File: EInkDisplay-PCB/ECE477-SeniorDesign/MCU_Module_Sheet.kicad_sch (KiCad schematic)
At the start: 25 parts, among them SW1 SW_Push_Dual_x2, U3 STM32L496ZGTxP, Y1 32.768kHz

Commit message: 0805
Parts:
- C19: footprint (none) -> Capacitor_SMD:C_0805_2012Metric_Pad1.18x1.45mm_HandSolder
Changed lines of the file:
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@@
 			)
 		)
-		(property "Footprint" ""
+		(property "Footprint" "Capacitor_SMD:C_0805_2012Metric_Pad1.18x1.45mm_HandSolder"
 			(at 179.07 34.29 0)
 			(effects

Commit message: change
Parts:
- added J7: Conn_01x05, symbol Connector_Generic:Conn_01x05
- ABS04W-32.768KHZ-4-D2-T5: renamed from Y1; footprint (none) -> PCB_Lib:XTAL_ABS04W-32.768KHZ-4-D2-T5
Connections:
- net NRST: now also J7.3 (Pin_3)
- net SWDIO: now reaches U3.105 (PA13)
- net SWDIO: now also J7.4 (Pin_4)
- net SWCLK: now reaches U3.109 (PA14)
- net SWCLK: now also J7.5 (Pin_5)

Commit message: push
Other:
- note added: "consider pull up"
- note removed: "force reset"
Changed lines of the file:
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@@
 		)
 	)
-	(text "force reset\n"
+	(text "consider pull up"
 		(exclude_from_sim no)
 		(at 143.764 44.958 0)

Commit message: Lotta changes
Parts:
- removed SW1: SW_Push_Dual_x2, symbol Switch:SW_Push_Dual_x2
- added J8: Conn_01x05, symbol Connector_Generic:Conn_01x05
- added TP17, TP18, TP19, TP20, TP21, TP22, TP23, TP24, TP25, TP26, TP27, TP28, TP29, TP30, TP31, TP32: ~, symbol Connector:TestPoint
- added U7: PTS526 SK15 SMTR2 LFS, PCB_Lib:PTS256, symbol EinkComponentLibrary:PTS526_SK15_SMTR2_LFS
- C1, C10, C11, C12, C13, C14, C15, C16, C17, C18, C2, C20, C3, C4, C9: footprint (none) -> Capacitor_SMD:C_0805_2012Metric_Pad1.18x1.45mm_HandSolder
- C28, C29: value 20pF -> 4pF; footprint (none) -> Capacitor_SMD:C_0805_2012Metric_Pad1.18x1.45mm_HandSolder
- SWBOOT0: value SW_SPDT -> PCM12SMTR; footprint (none) -> PCB_Lib:PCM12SMTR_CNK
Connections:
- net GND: now also U7.2
- net NRST: now also U7.1
- net button1: now also TP30.1
- net button2: now also TP31.1
- net button3: now also TP32.1
- net Extra_3: now reaches U3.1 (PE2)
- net Extra_3: now also J8.3 (Pin_3), TP27.1
- net USART2_TX: now reaches U3.119 (PD5)
- net USART2_TX: now also TP21.1
- net USART2_RX: now reaches U3.122 (PD6)
- net USART2_RX: now also TP22.1
- net SPI3_SCK: now reaches U3.124 (PG9)
- net SPI3_SCK: now also TP17.1
- net SPI3_MISO: now reaches U3.125 (PG10)
- net SPI3_MISO: now also TP18.1
- net SPI3_MOSI: now reaches U3.126 (PG11)
- net SPI3_MOSI: now also TP19.1
- net SPI3_NSS: now reaches U3.127 (PG12)
- net SPI3_NSS: now also TP20.1
- net Extra_1: now reaches U3.140 (PE0)
- net Extra_1: now also J8.1 (Pin_1), TP25.1
- net Extra_2: now reaches U3.141 (PE1)
- net Extra_2: now also J8.2 (Pin_2), TP26.1
- net Extra_4: now reaches U3.2 (PE3)
- net Extra_4: now also J8.4 (Pin_4), TP28.1
- net Extra_5: now reaches U3.3 (PE4)
- net Extra_5: now also J8.5 (Pin_5), TP29.1
- net I2C4_SCL: now reaches U3.81 (PD12)
- net I2C4_SCL: now also TP23.1
- net I2C4_SDA: now reaches U3.82 (PD13)
- net GPIO_1 renamed I2C2_SDA
- net GPIO_2 renamed I2C2_SCL
- no-connect marks 90 -> 79
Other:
- note added: "Extra Comms"
- note added: "Extra GPIOs"
- note added: "Extra SPI"
- note added: "Programming Header"
- moved on the sheet: J7

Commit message: onto PCB
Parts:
- removed ABS04W-32.768KHZ-4-D2-T5: 32.768kHz, PCB_Lib:XTAL_ABS04W-32.768KHZ-4-D2-T5, symbol Device:Crystal
- removed TP24: ~, symbol Connector:TestPoint
- added Y1: Y1, PCB_Lib:XTAL_ABS04W-32.768KHZ-4-D2-T5, symbol Device:Crystal_GND24_Small
- C1, C10, C11, C12, C13, C14, C15, C17, C18, C19, C2, C3, C4, C9: footprint Capacitor_SMD:C_0805_2012Metric_Pad1.18x1.45mm_HandSolder -> Capacitor_SMD:C_0603_1608Metric_Pad1.08x0.95mm_HandSolder
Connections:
- net GND: now also Y1.2
- net GPIO_3: now also U3.80 (PD11); no longer U3.12 (PF2)
- net GPIO_4: now also U3.79 (PD10); no longer U3.13 (PF3)
- net GPIO_5: now also U3.78 (PD9); no longer U3.14 (PF4)
- net GPIO_6: now also U3.77 (PD8); no longer U3.15 (PF5)
- net I2C2_SCL: now also TP23.1, U3.81 (PD12); no longer U3.11 (PF1)
- net I2C2_SDA: now also U3.82 (PD13); no longer U3.10 (PF0)
- net I2C4_SCL: now also U3.11 (PF1); no longer TP23.1, U3.81 (PD12)
- net I2C4_SDA: now also U3.10 (PF0); no longer U3.82 (PD13)
- net at C28.2, U3.23 (PH0): now also Y1.1
- net at C29.2, U3.24 (PH1): now also Y1.3
- no-connect marks 79 -> 80
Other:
- note removed: "Extra Comms"
- moved on the sheet: C28, C29, U7

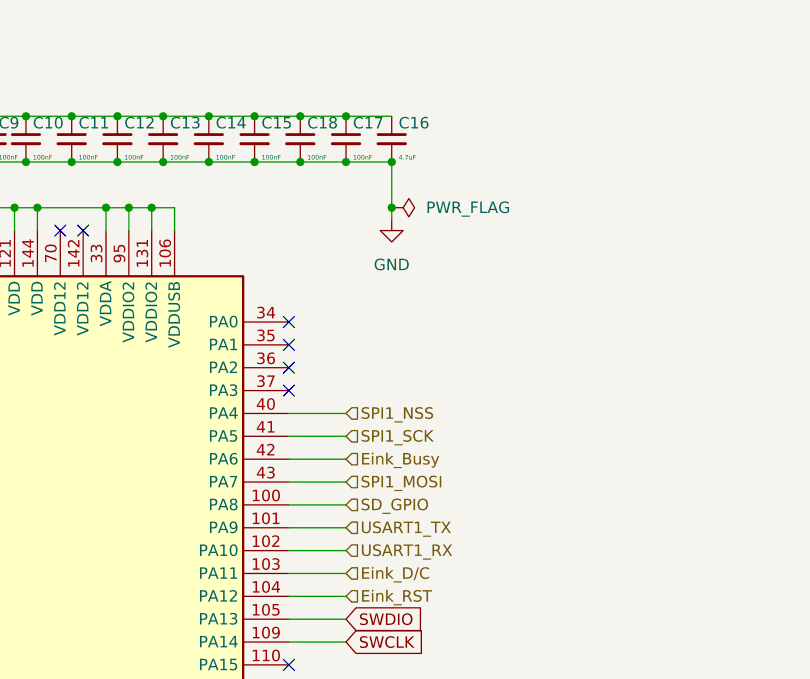
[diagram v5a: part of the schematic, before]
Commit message: SD card updates
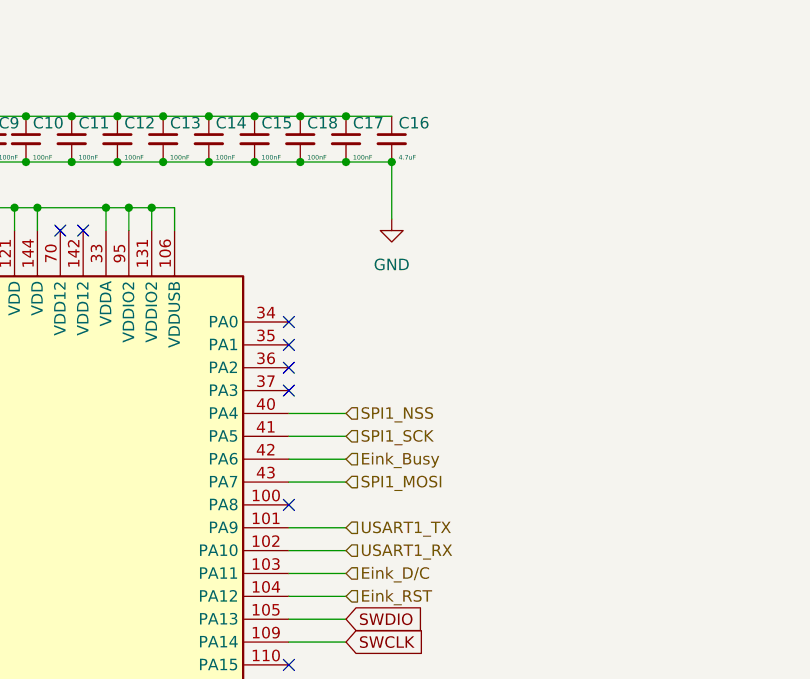
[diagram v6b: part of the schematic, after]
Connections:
- net SD_GPIO: no longer names the net of U3.100 (PA8)
- no-connect marks 80 -> 81
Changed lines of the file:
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@@
 	)
 	(junction
-		(at 243.84 41.91)
-		(diameter 0)
-		(color 0 0 0 0)
-	)
-	(junction
 		(at 121.92 111.76)
 		(diameter 0)
@@
 	)
 	(no_connect
+		(at 232.41 74.93)
+	)
+	(no_connect
 		(at 166.37 135.89)
 	)
@@
 	(wire
 		(pts
-			(xy 243.84 36.83) (xy 243.84 41.91)
+			(xy 243.84 36.83) (xy 243.84 43.18)
 		)
 		(stroke
@@
 	(wire
 		(pts
-			(xy 232.41 74.93) (xy 238.76 74.93)
-		)
-		(stroke
-			(width 0)
-			(type default)
-		)
-	)
-	(wire
-		(pts
 			(xy 232.41 130.81) (xy 241.3 130.81)
 		)
@@
 	(wire
 		(pts
-			(xy 243.84 41.91) (xy 243.84 43.18)
-		)
-		(stroke
-			(width 0)
-			(type default)
-		)
-	)
-	(wire
-		(pts
 			(xy 146.05 64.77) (xy 146.05 67.31)
 		)
@@
 		)
 	)
-	(hierarchical_label "SD_GPIO"
-		(shape input)
-		(at 238.76 74.93 0)
-		(effects
-			(font
-				(size 1.27 1.27)
-			)
-			(justify left)
-		)
-	)
 	(hierarchical_label "button1"
 		(shape input)
@@
 					(unit 1)
 				)
-			)
-		)
-	)
-	(symbol
-		(lib_id "power:PWR_FLAG")
-		(at 243.84 41.91 270)
-		(unit 1)
-		(exclude_from_sim no)
-		(in_bom yes)
-		(on_board yes)
-		(dnp no)
-		(fields_autoplaced yes)
-		(property "Reference" "#FLG01"
-			(at 245.745 41.91 0)
-			(effects
-				(font
-					(size 1.27 1.27)
-				)
-				(hide yes)
-			)
-		)
-		(property "Value" "PWR_FLAG"
-			(at 247.65 41.9099 90)
-			(effects
-				(font
-					(size 1.27 1.27)
-				)
-				(justify left)
-			)
-		)
-		(property "Footprint" ""
-			(at 243.84 41.91 0)
-			(effects
-				(font
-					(size 1.27 1.27)
-				)
-				(hide yes)
-			)
-		)
-		(property "Datasheet" "~"
-			(at 243.84 41.91 0)
-			(effects
-				(font
-					(size 1.27 1.27)
-				)
-				(hide yes)
-			)
-		)
-		(property "Description" "Special symbol for telling ERC where power comes from"
-			(at 243.84 41.91 0)
-			(effects
-				(font
-					(size 1.27 1.27)
-				)
-				(hide yes)
-			)
-		)
-		(pin "1"
-		)
-		(instances
-			(project ""
-				(path "/527ae649-08be-4368-9cf9-441ebba18eca/a47b6934-98dd-4056-b1df-1ab751d1c2a0"
-					(reference "#FLG01")
-					(unit 1)
-				)

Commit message: whole lotta changes
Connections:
- net Extra_3: now also TP32.1, U3.45 (PC5); no longer TP27.1, U3.1 (PE2)
- net Extra_4: now also TP31.1, U3.44 (PC4); no longer TP28.1, U3.2 (PE3)
- net Extra_5: now also TP30.1, U3.29 (PC3); no longer TP29.1, U3.3 (PE4)
- net button1: now also TP29.1, U3.3 (PE4); no longer TP30.1, U3.29 (PC3)
- net button2: now also TP28.1, U3.2 (PE3); no longer TP31.1, U3.44 (PC4)
- net button3: now also TP27.1, U3.1 (PE2); no longer TP32.1, U3.45 (PC5)

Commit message: pushing
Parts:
- removed J8: Conn_01x05, symbol Connector_Generic:Conn_01x05
- added J2: Conn_01x05_Pin, Connector_PinHeader_1.00mm:PinHeader_1x05_P1.00mm_Vertical, symbol Connector:Conn_01x05_Pin
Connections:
- net Extra_1: now also TP26.1, U3.141 (PE1), J2.5 (Pin_5); no longer TP25.1, U3.140 (PE0)
- net Extra_2: now also TP25.1, U3.140 (PE0), J2.4 (Pin_4); no longer TP26.1, U3.141 (PE1)
- net Extra_3: now also U3.138 (PB8), J2.3 (Pin_3)
- net Extra_4: now also U3.136 (PB7), J2.2 (Pin_2)
- net Extra_5: now also U3.135 (PB6), J2.1 (Pin_1)
- net button1: now also TP27.1, U3.1 (PE2); no longer TP29.1, U3.3 (PE4)
- net button3: now also TP29.1, U3.3 (PE4); no longer TP27.1, U3.1 (PE2)
- no-connect marks 81 -> 78
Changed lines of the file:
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@@
 	)
 	(junction
+		(at 241.3 212.09)
+		(diameter 0)
+		(color 0 0 0 0)
+	)
+	(junction
 		(at 179.07 31.75)
 		(diameter 0)
@@
 	)
 	(junction
-		(at 241.3 212.09)
-		(diameter 0)
-		(color 0 0 0 0)
-	)
-	(junction
 		(at 218.44 36.83)
 		(diameter 0)
@@
 	)
 	(no_connect
-		(at 232.41 113.03)
-	)
-	(no_connect
 		(at 232.41 173.99)
 	)
@@
 	)
 	(no_connect
-		(at 232.41 115.57)
-	)
-	(no_connect
 		(at 232.41 219.71)
 	)
@@
 	)
 	(no_connect
-		(at 232.41 118.11)
-	)
-	(no_connect
 		(at 166.37 128.27)
 	)
@@
 	(wire
 		(pts
+			(xy 237.49 115.57) (xy 237.49 111.76)
+		)
+		(stroke
+			(width 0)
+			(type default)
+		)
+	)
+	(wire
+		(pts
 			(xy 187.96 31.75) (xy 191.77 31.75)
 		)
@@
 	(wire
 		(pts
+			(xy 232.41 113.03) (xy 236.22 113.03)
+		)
+		(stroke
+			(width 0)
+			(type default)
+		)
+	)
+	(wire
+		(pts
 			(xy 179.07 31.75) (xy 184.15 31.75)
 		)
@@
 	(wire
 		(pts
+			(xy 232.41 118.11) (xy 241.3 118.11)
+		)
+		(stroke
+			(width 0)
+			(type default)
+		)
+	)
+	(wire
+		(pts
 			(xy 223.52 36.83) (xy 228.6 36.83)
 		)
@@
 	(wire
 		(pts
+			(xy 237.49 111.76) (xy 241.3 111.76)
+		)
+		(stroke
+			(width 0)
+			(type default)
+		)
+	)
+	(wire
+		(pts
 			(xy 133.35 88.9) (xy 130.81 88.9)
 		)
@@
 	(wire
 		(pts
+			(xy 236.22 113.03) (xy 236.22 109.22)
+		)
+		(stroke
+			(width 0)
+			(type default)
+		)
+	)
+	(wire
+		(pts
 			(xy 138.43 54.61) (xy 146.05 54.61)
 		)
@@
 	(wire
 		(pts
+			(xy 236.22 109.22) (xy 241.3 109.22)
+		)
+		(stroke
+			(width 0)
+			(type default)
+		)
+	)
+	(wire
+		(pts
 			(xy 133.35 64.77) (xy 133.35 67.31)
 		)
@@
 	(wire
 		(pts
+			(xy 232.41 212.09) (xy 241.3 212.09)
+		)
+		(stroke
+			(width 0)
+			(type default)
+		)
+	)
+	(wire
+		(pts
 			(xy 232.41 146.05) (xy 237.49 146.05)
 		)
@@
 	(wire
 		(pts
-			(xy 232.41 212.09) (xy 241.3 212.09)
+			(xy 241.3 118.11) (xy 241.3 114.3)
 		)
 		(stroke
@@
 	(wire
 		(pts
+			(xy 232.41 115.57) (xy 237.49 115.57)
+		)
+		(stroke
+			(width 0)
+			(type default)
+		)
+	)
+	(wire
+		(pts
 			(xy 238.76 31.75) (xy 243.84 31.75)
 		)
@@
 		)
 	)
+	(global_label "Extra_5"
+		(shape input)
+		(at 241.3 109.22 0)
+		(fields_autoplaced yes)
+		(effects
+			(font
+				(size 1.27 1.27)
+			)
+			(justify left)
+		)
+		(property "Intersheetrefs" "${INTERSHEET_REFS}"
+			(at 251.3003 109.22 0)
+			(effects
+				(font
+					(size 1.27 1.27)
+				)
+				(justify left)
+				(hide yes)
+			)
+		)
+	)
 	(global_label "USART2_RX"
 		(shape input)
@@
 		)
 	)
-	(global_label "Extra_2"
+	(global_label "Extra_1"
 		(shape input)
 		(at 156.21 163.83 180)
@@
 		)
 	)
-	(global_label "Extra_1"
+	(global_label "Extra_2"
 		(shape input)
 		(at 156.21 161.29 180)
@@
 	(global_label "Extra_3"
 		(shape input)
+		(at 241.3 114.3 0)
+		(fields_autoplaced yes)
+		(effects
+			(font
+				(size 1.27 1.27)
+			)
+			(justify left)
+		)
+		(property "Intersheetrefs" "${INTERSHEET_REFS}"
+			(at 251.3003 114.3 0)
+			(effects
+				(font
+					(size 1.27 1.27)
+				)
+				(justify left)
+				(hide yes)
+			)
+		)
+	)
+	(global_label "Extra_3"
+		(shape input)
 		(at 256.54 151.13 0)
 		(fields_autoplaced yes)
@@
 		)
 	)
+	(global_label "Extra_4"
+		(shape input)
+		(at 241.3 111.76 0)
+		(fields_autoplaced yes)
+		(effects
+			(font
+				(size 1.27 1.27)
+			)
+			(justify left)
+		)
+		(property "Intersheetrefs" "${INTERSHEET_REFS}"
+			(at 251.3003 111.76 0)
+			(effects
+				(font
+					(size 1.27 1.27)
+				)
+				(justify left)
+				(hide yes)
+			)
+		)
+	)
 	(global_label "Extra_2"
 		(shape input)
@@
 		)
 	)
-	(hierarchical_label "button1"
+	(hierarchical_label "button3"
 		(shape input)
 		(at 156.21 171.45 180)
@@
 		)
 	)
-	(hierarchical_label "I2C2_SCL"
-		(shape input)
-		(at 281.94 212.09 0)
-		(effects
-			(font
-				(size 1.27 1.27)
-			)
-			(justify left)
-		)
-	)
 	(hierarchical_label "USART1_RX"
 		(shape input)
@@
 		)
 	)
-	(hierarchical_label "button3"
+	(hierarchical_label "button1"
 		(shape input)
 		(at 156.21 166.37 180)
@@
 		)
 	)
+	(hierarchical_label "I2C2_SCL"
+		(shape input)
+		(at 281.94 212.09 0)
+		(effects
+			(font
+				(size 1.27 1.27)
+			)
+			(justify left)
+		)
+	)
 	(hierarchical_label "USART1_TX"
 		(shape input)
@@
 	)
 	(symbol
-		(lib_id "Connector_Generic:Conn_01x05")
-		(at 86.36 163.83 0)
-		(unit 1)
-		(exclude_from_sim no)
-		(in_bom yes)
-		(on_board yes)
-		(dnp no)
-		(fields_autoplaced yes)
-		(property "Reference" "J8"
-			(at 88.9 162.5599 0)
-			(effects
-				(font
-					(size 1.27 1.27)
-				)
-				(justify left)
-			)
-		)
-		(property "Value" "Conn_01x05"
-			(at 88.9 165.0999 0)
-			(effects
-				(font
-					(size 1.27 1.27)
-				)
-				(justify left)
-			)
-		)
-		(property "Footprint" ""
-			(at 86.36 163.83 0)
-			(effects
-				(font
-					(size 1.27 1.27)
-				)
-				(hide yes)
-			)
-		)
-		(property "Datasheet" "~"
-			(at 86.36 163.83 0)
-			(effects
-				(font
-					(size 1.27 1.27)
-				)
-				(hide yes)
-			)
-		)
-		(property "Description" "Generic connector, single row, 01x05, script generated (kicad-library-utils/schlib/autogen/connector/)"
-			(at 86.36 163.83 0)
-			(effects
-				(font
-					(size 1.27 1.27)
-				)
-				(hide yes)
-			)
-		)
-		(pin "2"
-		)
-		(pin "1"
-		)
-		(pin "3"
-		)
-		(pin "4"
-		)
-		(pin "5"
-		)
-		(instances
-			(project "ECE477-SeniorDesign"
-				(path "/527ae649-08be-4368-9cf9-441ebba18eca/a47b6934-98dd-4056-b1df-1ab751d1c2a0"
-					(reference "J8")
-					(unit 1)
-				)
-			)
-		)
-	)
-	(symbol
 		(lib_id "power:GND")
 		(at 134.62 24.13 180)
@@
 					(unit 1)
 				)
+			)
+		)
+	)
+	(symbol
+		(lib_id "Connector:Conn_01x05_Pin")
+		(at 86.36 163.83 180)
+		(unit 1)
+		(exclude_from_sim no)
+		(in_bom yes)
+		(on_board yes)
+		(dnp no)
+		(fields_autoplaced yes)
+		(property "Reference" "J2"
+			(at 87.63 162.5599 0)
+			(effects
+				(font
+					(size 1.27 1.27)
+				)
+				(justify right)
+			)
+		)
+		(property "Value" "Conn_01x05_Pin"
+			(at 87.63 165.0999 0)
+			(effects
+				(font
+					(size 1.27 1.27)
+				)
+				(justify right)
+			)
+		)
+		(property "Footprint" "Connector_PinHeader_1.00mm:PinHeader_1x05_P1.00mm_Vertical"
+			(at 86.36 163.83 0)
+			(effects
+				(font
+					(size 1.27 1.27)
+				)
+				(hide yes)
+			)
+		)
+		(property "Datasheet" "~"
+			(at 86.36 163.83 0)
+			(effects
+				(font
+					(size 1.27 1.27)
+				)
+				(hide yes)
+			)
+		)
+		(property "Description" "Generic connector, single row, 01x05, script generated"
+			(at 86.36 163.83 0)
+			(effects
+				(font
+					(size 1.27 1.27)
+				)
+				(hide yes)
+			)
+		)
+		(pin "4"
+		)
+		(pin "5"
+		)
+		(pin "3"
+		)
+		(pin "2"
+		)
+		(pin "1"
+		)
+		(instances
+			(project ""
+				(path "/527ae649-08be-4368-9cf9-441ebba18eca/a47b6934-98dd-4056-b1df-1ab751d1c2a0"
+					(reference "J2")
+					(unit 1)
+				)
